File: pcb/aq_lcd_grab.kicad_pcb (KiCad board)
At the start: 4 copper layers, 32 x 50 mm, 24 parts, among them J1 Conn_01x39_Socket, J2 Conn_01x39_Socket, J3 Conn_01x03_Socket, J5 Conn_01x03_Pin, U1 STM32F103C8Tx, U2 Conn_01x14

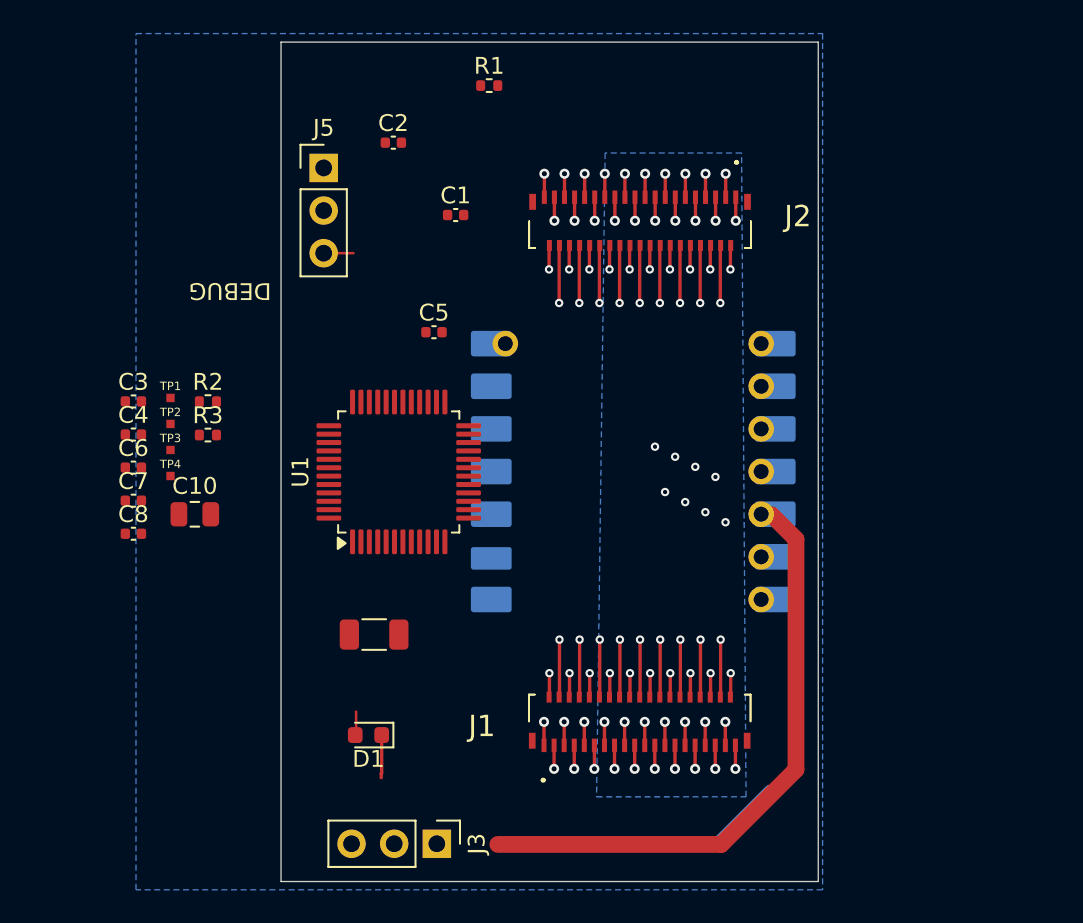
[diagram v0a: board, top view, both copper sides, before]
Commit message: Rename script to route_lcd_bus.py; add DC escape via and width filter
The script does more than straighten now — it adds escape vias and routes
even-DB nets around them. Rename matches. Other changes:

- Filter to width-0.1 segments so hand-routed traces (other widths) on
  the flex pass-through nets are left untouched.
- Add EXTRA_ESCAPE_VIAS hook for non-DB nets, currently used to place
  DC just above DB15 (the highest staggered escape via). y is computed
  from the layout constants so it tracks ESCAPE_Y_STEP / ROW_GAP edits.
- Pre-compute planned escape via positions into all_vias before the
  routing loop so first-run routing knows to dodge them.

Co-Authored-By: Claude Opus 4.7 (1M context) <noreply@anthropic.com>
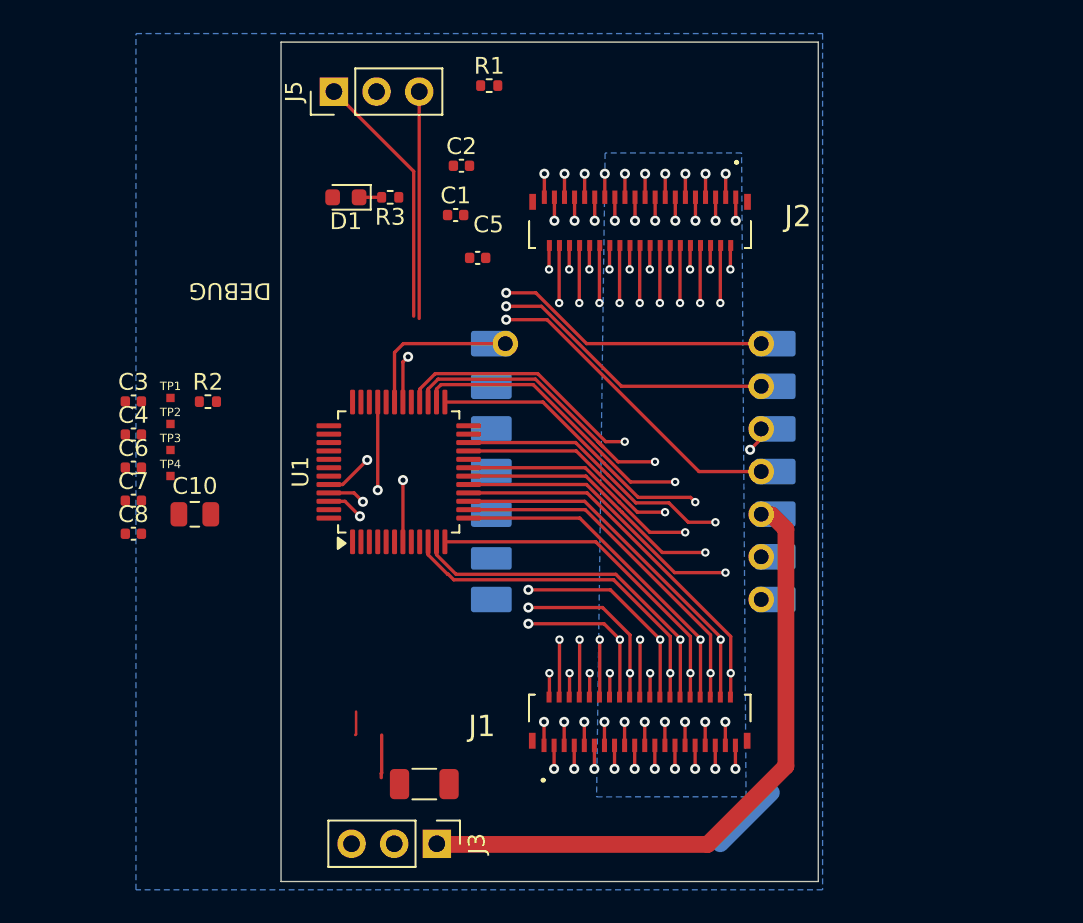
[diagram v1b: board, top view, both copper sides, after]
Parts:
- moved D1 32.1 mm to (54.7, 34.6)
- moved R3 17.8 mm to (57.3, 34.6), turned to 180 degrees
- moved C11 9.39 mm to (59.3, 69.6)
- moved C5 5.14 mm to (62.5, 38.3)
- moved J5 4.59 mm to (53.9, 28.3), turned to 90 degrees
- moved C2 4.28 mm to (61.5, 32.8)
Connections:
- U1 pad 10: DB0 -> DB12
- U1 pad 11: DB1 -> DB10
- U1 pad 12: DB2 -> DB8
- U1 pad 13: DB3 -> DB6
- U1 pad 15: DB5 -> DB2
- U1 pad 16: DB6 -> DB0
- U1 pad 17: DB7 -> DB1
- U1 pad 18: DC -> DB5
- U1 pad 19: CS -> DB9
- U1 pad 21: DB10 -> DB13
- U1 pad 22: DB11 -> DB3
- U1 pad 25: DB12 -> DB7
- U1 pad 26: DB13 -> DB11
- U1 pad 27: DB14 -> DB15
- U1 pad 28: DB15 -> DC
- U1 pad 45: DB8 -> DB14
- U1 pad 46: DB9 -> CS
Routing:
- net PIC32_RESET: track 0.00 -> 46.3 mm, vias 0 -> 1
- net NRST: track 0.00 -> 34.9 mm, vias 0 -> 2
- net BOOT0: track 0.00 -> 33.7 mm, vias 0 -> 2
- net UART_STM_TX: track 0.00 -> 26.7 mm, vias 0 -> 2
- net WR: track 26.9 -> 53.1 mm, vias 2 -> 4
- net DB14: track 26.8 -> 50.1 mm, vias 2 -> 4
- net DB0: track 27.0 -> 48.4 mm
- net CS: track 26.5 -> 47.4 mm, vias 2 -> 4
- net DB4: track 27.2 -> 47.0 mm
- net DB12: track 27.2 -> 46.6 mm
- net DB8: track 27.2 -> 46.3 mm
- net DB2: track 26.8 -> 45.3 mm
- net DB11: track 36.1 -> 53.6 mm
- net DB1: track 36.1 -> 53.6 mm
- net DB10: track 26.8 -> 44.2 mm
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
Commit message: SKiDL: shuffle DBn-to-pin assignments, document order is arbitrary
Reassigns DBn pins on the STM32 capture tap and moves the resulting
shallow-band traces to B.Cu. The DB ordering is arbitrary on the wire —
the firmware permutes them in software per docs/pcb_spec.md Q13.

Co-Authored-By: Claude Opus 4.7 (1M context) <noreply@anthropic.com>
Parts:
- moved C10 18.6 mm to (59.4, 66.0)
- moved C6 5.16 mm to (37.3, 52.9)
- moved C7 4.73 mm to (39.1, 56.4)
- moved C8 4.19 mm to (45.2, 57.4)
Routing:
- net CS: track 47.4 -> 50.3 mm
- net N$1: track 3.84 -> 1.29 mm
- net WR: track 53.1 -> 55.5 mm
- net DB14: track 50.1 -> 51.9 mm
- net LED_STATUS: track 1.42 -> 0.00 mm
- added copper zone on In1.Cu, net GND
- removed copper zone on B.Cu, net GND

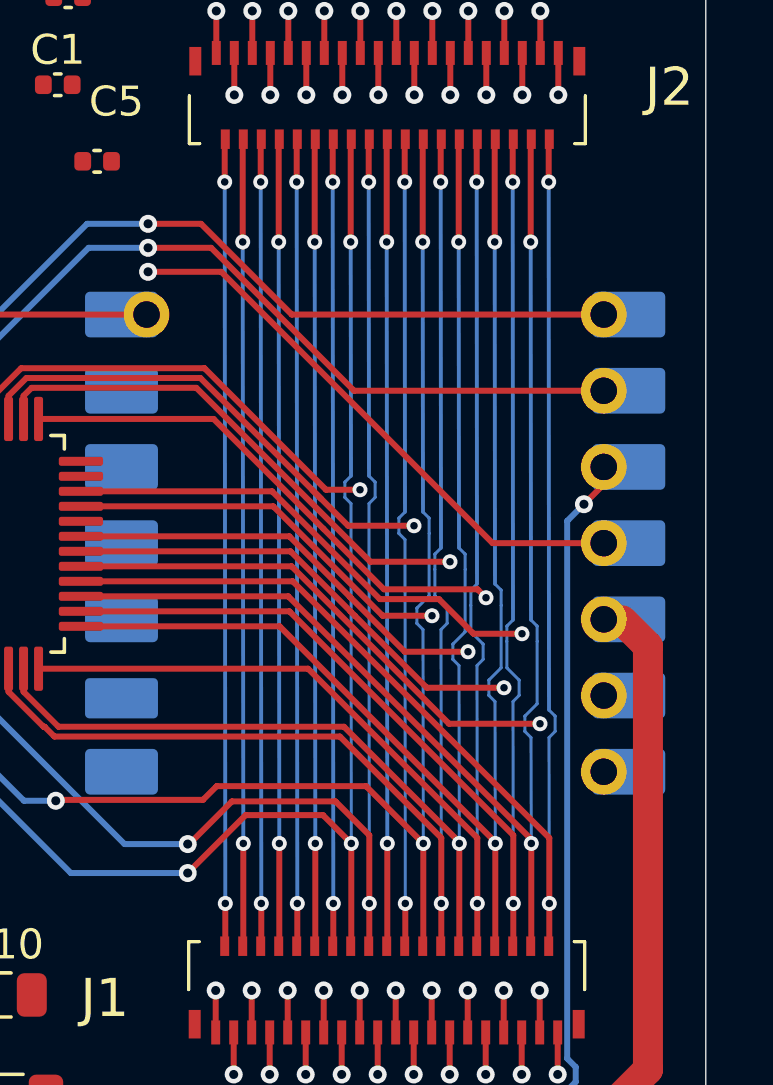
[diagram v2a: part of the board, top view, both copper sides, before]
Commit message: route_lcd_bus: tighter doglegs, B.Cu width 0.13, flex-pair tolerance
- Per-obstacle dogleg returns to column between obstacles, so the trace
  doesn't camp at offset longer than needed.
- SCRIPT_LAYER_WIDTH lets each layer pick its trace width; B.Cu uses 0.13
  to satisfy outer-layer DRC. Legacy 0.1-width segments on script layers
  are still recognized and rewritten at the new width.
- Tightened flex-band y tolerance (0.001 mm) so hand-placed off-bus vias
  near a band y aren't mistaken for flex pass-through vias (was breaking
  WR routing).

Co-Authored-By: Claude Opus 4.7 (1M context) <noreply@anthropic.com>
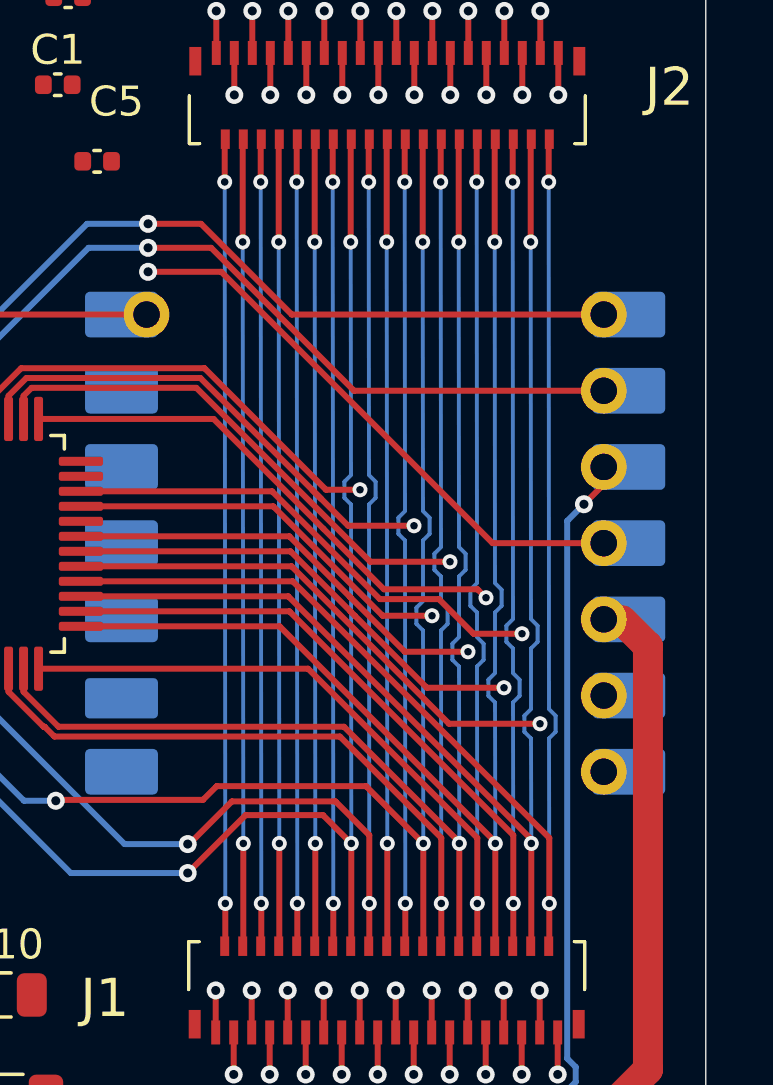
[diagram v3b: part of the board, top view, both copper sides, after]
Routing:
- net (no net): track 0.00 -> 3.93 mm

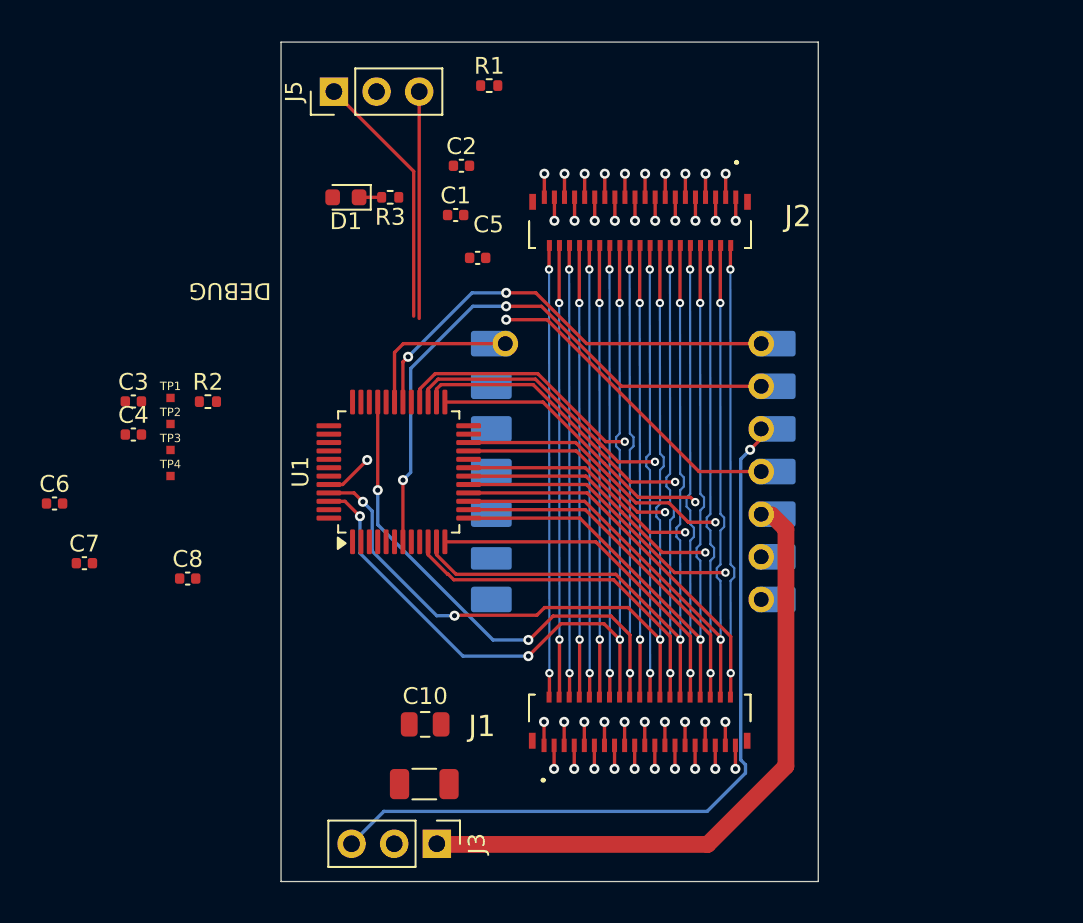
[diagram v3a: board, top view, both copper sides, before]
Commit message: PCB: layout refresh after netlist re-import, relax zone fill rules
Re-import of the updated SKiDL netlist into KiCad: refdes shuffling
on the STM32 decoupling caps (C2..C5 reassigned by tag), placement
adjustments, and a few extra components landing in the layout.

Zone fill defaults bumped from 0.15 mm to 0.3 mm for both
min_clearance and min_thickness — comfortable headroom over JLCPCB's
standard 6/6 mil (~0.15 mm) capability so fills don't get thin
filaments at narrow gaps.

Co-Authored-By: Claude Opus 4.7 (1M context) <noreply@anthropic.com>
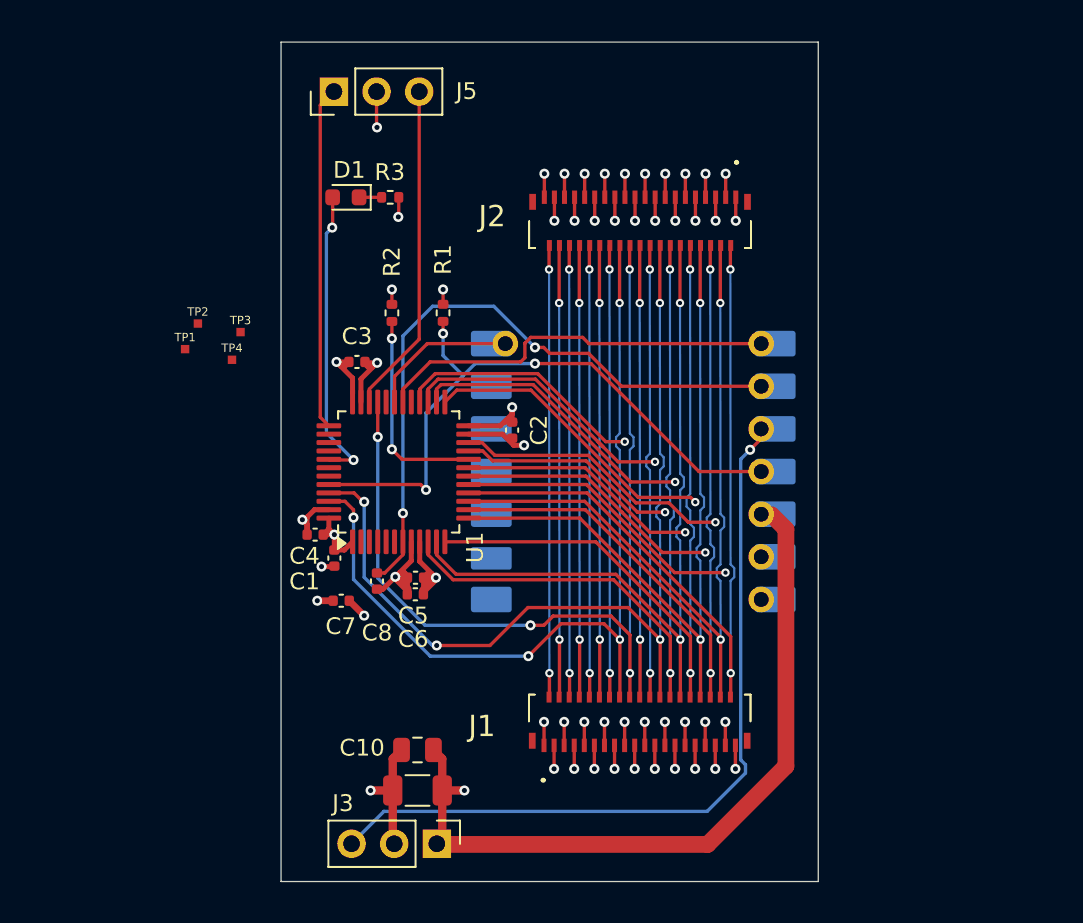
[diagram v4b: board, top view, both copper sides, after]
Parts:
- removed the C2 at (61.5, 32.8)
- added C5: 100n, Capacitor_SMD:C_0402_1005Metric, F.Cu at (58.8, 57.3)
- moved C2 22.6 mm to (64.6, 48.5), turned to -90 degrees
- moved C6 22.2 mm to (58.8, 58.3), turned to 180 degrees
- moved C1 21.7 mm to (54.0, 56.1), turned to -90 degrees
- moved C4 19.1 mm to (52.8, 54.7), turned to 180 degrees
- moved C7 15.5 mm to (54.4, 58.7)
- moved C3 14.0 mm to (55.3, 44.5)
- moved R1 13.8 mm to (60.5, 41.5), turned to 90 degrees
- moved R2 12.2 mm to (57.4, 41.5), turned to 90 degrees
- moved C8 11.3 mm to (56.5, 57.5), turned to -90 degrees
- moved TP3 8.17 mm to (48.4, 42.7)
- moved TP4 7.83 mm to (47.9, 44.3)
- moved TP2 6.20 mm to (45.8, 42.2)
- moved TP1 3.03 mm to (45.1, 43.7)
- moved C10 1.59 mm to (58.9, 67.6), turned to 180 degrees
- moved C11 0.56 mm to (58.9, 70.0)
- renumbered C3 to C2, C4 to C3, C5 to C4
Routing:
- net GND: track 0.00 -> 31.1 mm, vias 0 -> 10
- net +3V3: track 38.1 -> 65.8 mm, vias 0 -> 7
- net LED_STATUS: track 0.00 -> 18.0 mm, vias 0 -> 2
- net BOOT1: track 0.00 -> 12.4 mm, vias 0 -> 2
- net SWDIO: track 13.5 -> 19.7 mm
- net SWCLK: track 15.3 -> 20.5 mm
- net BOOT0: track 33.7 -> 38.1 mm, vias 2 -> 3
- net +5V: track 4.31 -> 0.00 mm
- net NRST: track 34.9 -> 39.1 mm
- net (no net): track 3.93 -> 0.00 mm
- net DB14: track 52.0 -> 54.7 mm
- net UART_STM_TX: track 26.7 -> 24.0 mm, vias 2 -> 0
- net CS: track 50.3 -> 51.4 mm
- net WR: track 55.5 -> 56.7 mm
- net UART_STM_RX: track 9.77 -> 8.94 mm
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- added copper zone on In2.Cu, net +3V3
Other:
- board text removed: "DEBUG"

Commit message: Spec cleanup + add flex-GND/UART/5V-tap jumpers and 5V tap header
Spec: collapse a pile of recap-or-stale open questions (Q3/Q7/Q7b
table, Q8 form-factor, Q9 GND-pour, Q11 inductor, Q12 DMA recap,
Q13 fanout, Q14 SWO, Q16 RM0360) by either promoting the
load-bearing parts into the main spec or dropping them outright.
New main-spec sections: "Decoupling" under Power (promoted from Q7),
"Flex GND tie" under Display capture tap (promoted from Q18), and
a "Fallback if 3V3 headroom is insufficient" bullet under Power
(promoted from Q20). target (JLCPCB part sourcing) expanded from
flex-only to a full BOM cost review with a per-part table — the
LED was flagged as having moved out of the basic library and
similar drift is likely on other parts. Q19 (UART jumpers) dropped
since the SKiDL change is self-documenting. Open questions left:
Q6 (3V3 headroom), target (BOOT cost review), Q15 (Embassy), Q17
(bit-permutation table), Q21 (PIC32 reset). Stale RP2350-era
references in the Power section and other dead Q-refs cleaned out.

SKiDL: R10..R12 add 0 Ω jumpers tying GND_1/GND_18/GND_19 flex pins
to board GND, populated by default. R13/R14 add 0 Ω break jumpers
in series with UART_STM_TX/RX, splitting each line into STM32-side
and ESP32-side halves so the link can be opened during bring-up.
J4 adds a 2-pin 2.54 mm header on +5V/GND for the optional target
5V tap if the 3V3 headroom (Q6) turns out insufficient.

Co-Authored-By: Claude Opus 4.7 (1M context) <noreply@anthropic.com>
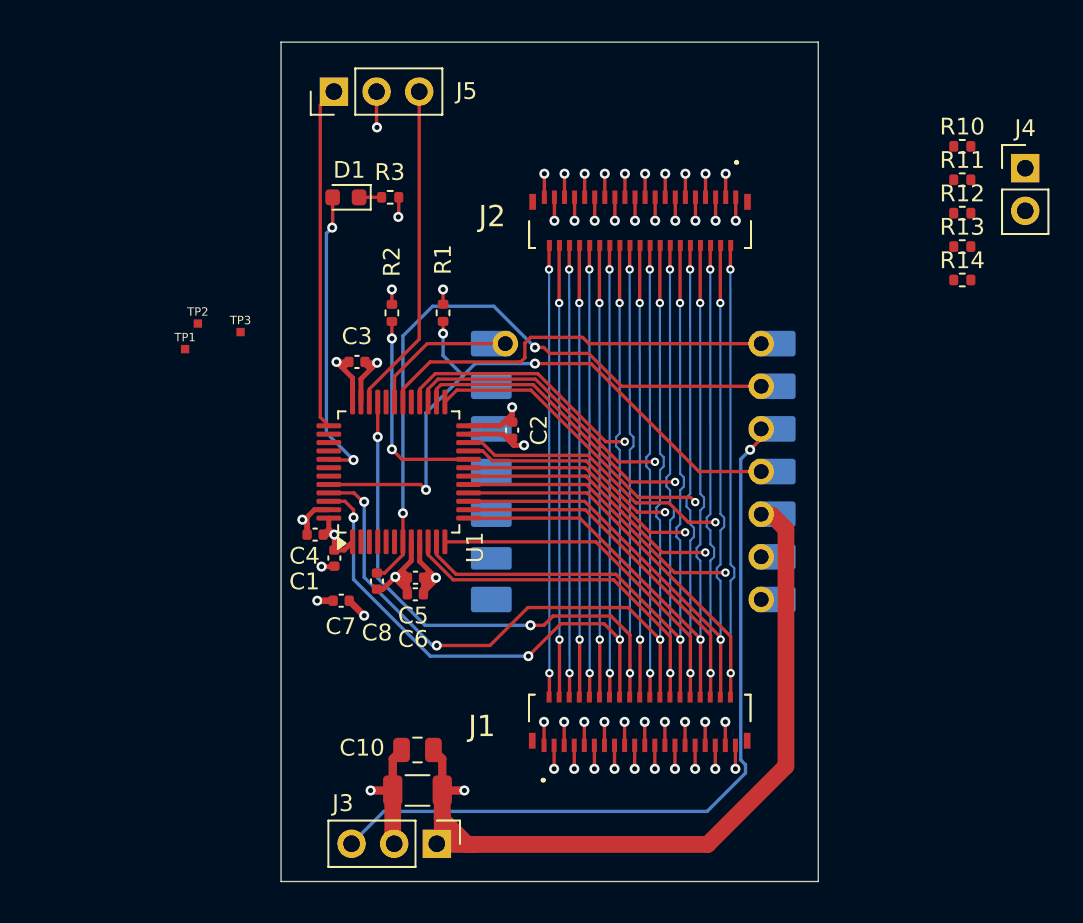
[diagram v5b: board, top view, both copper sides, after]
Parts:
- removed TP4: TestPoint, test_points:TestPoint_Pad_0.5x0.5mm
- added J4: Conn_01x02_Socket, Connector_PinHeader_2.54mm:PinHeader_1x02_P2.54mm_Vertical, F.Cu at (95.1, 32.9)
- added R10: 0, Resistor_SMD:R_0402_1005Metric, F.Cu at (91.4, 31.6)
- added R11: 0, Resistor_SMD:R_0402_1005Metric, F.Cu at (91.4, 33.6)
- added R12: 0, Resistor_SMD:R_0402_1005Metric, F.Cu at (91.4, 35.6)
- added R13: 0, Resistor_SMD:R_0402_1005Metric, F.Cu at (91.4, 37.6)
- added R14: 0, Resistor_SMD:R_0402_1005Metric, F.Cu at (91.4, 39.6)
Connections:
- TP1 pad 1: DB2 -> PB3
- TP2 pad 1: DB3 -> PB4
- TP3 pad 1: PB3 -> PB5
- U1 pad 2: (no net) -> LED_STATUS
- U1 pad 41: LED_STATUS -> PB5
- U2 pad 7: UART_STM_RX -> UART_ESP_TX
- U2 pad 8: UART_STM_TX -> UART_ESP_RX
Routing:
- net +3V3: track 65.8 -> 70.1 mm
